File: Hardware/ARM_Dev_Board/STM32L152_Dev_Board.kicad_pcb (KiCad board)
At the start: 2 copper layers, 65.3 x 24.9 mm, 21 parts, among them J1 SWD_Header, J2 Conn_01x20_Female, J3 Conn_01x22_Female, J4 Eurorack_10_pin_power, SW1 SW_Push, U1 STM32L451CCUx, U4 LM1117-3.3, Y1 Crystal

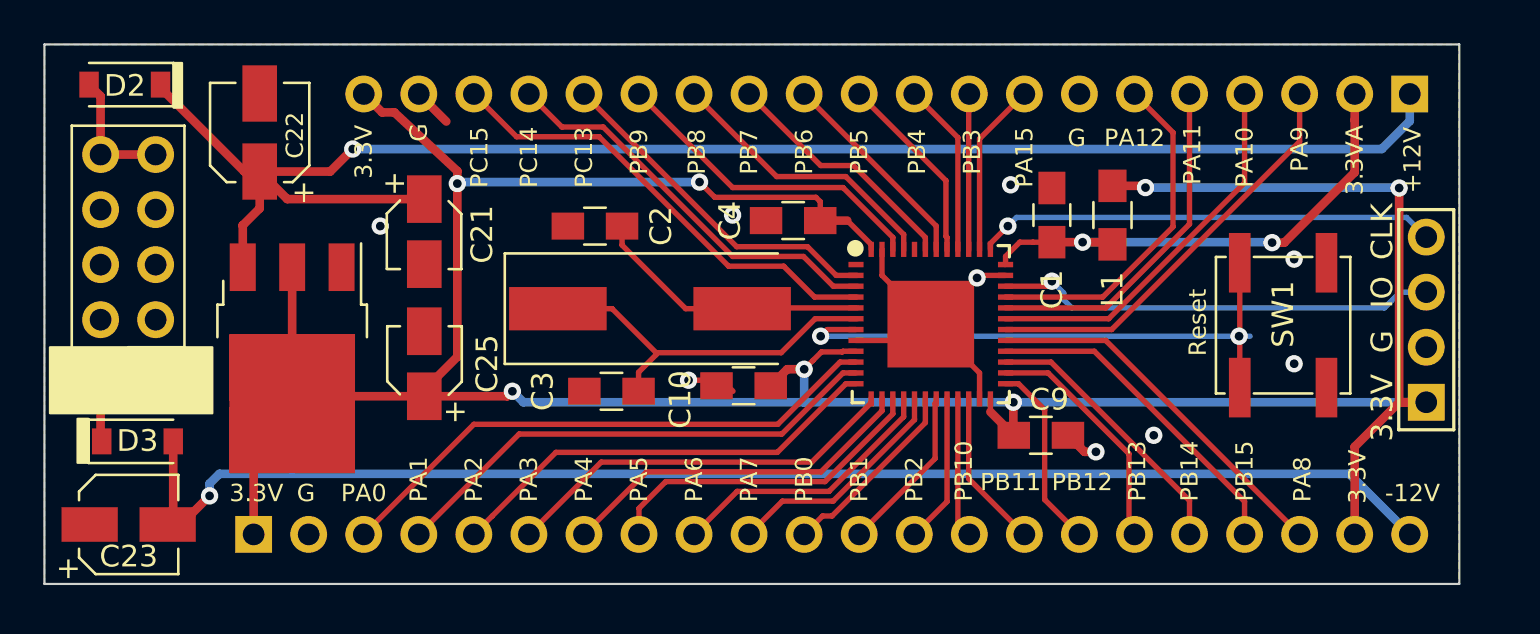
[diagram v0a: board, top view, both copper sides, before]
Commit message: Dev Board 1.1 layout finalised and gerbers sent to manufacturing
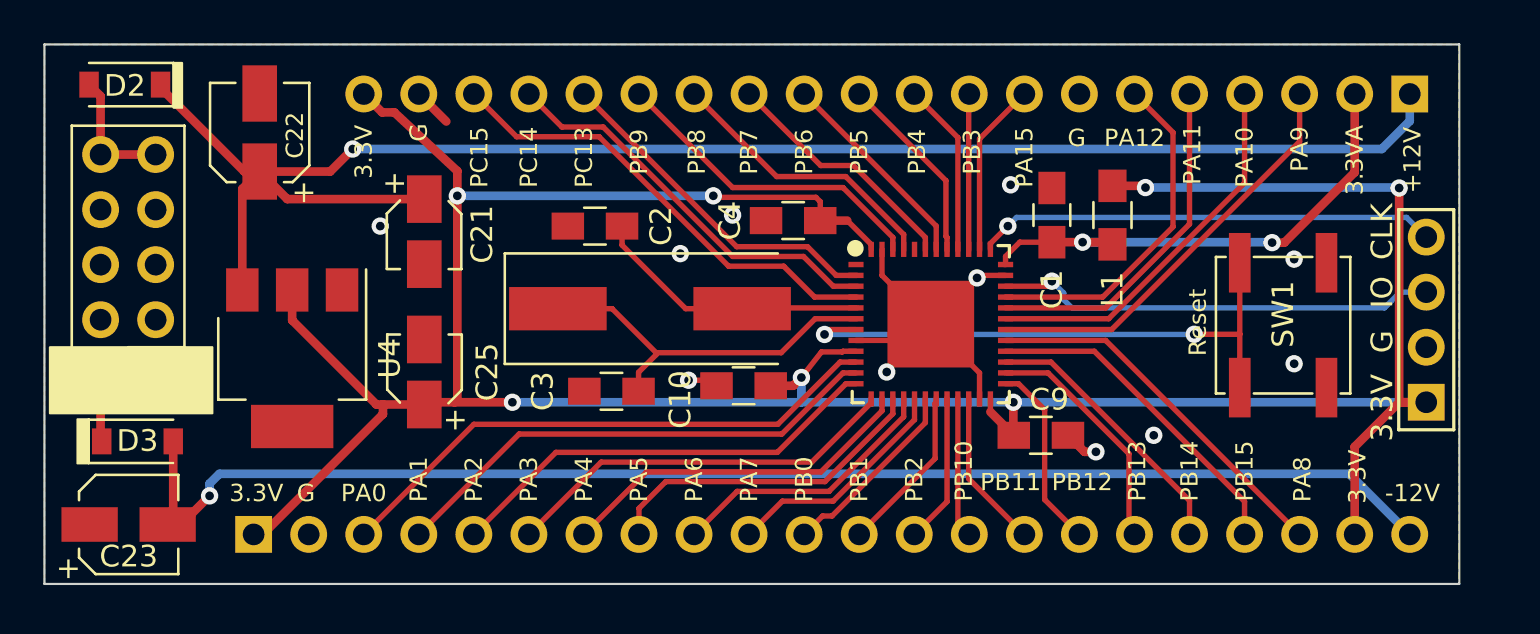
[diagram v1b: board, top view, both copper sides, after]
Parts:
- U4: footprint TO_SOT_Packages_SMD:TO-252-3_TabPin2 -> TO_SOT_Packages_SMD:SOT-223
- moved C25 0.38 mm to (160.3, 141.9)
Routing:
- net +3V3: track 146.3 -> 143.6 mm
- net VCC: track 74.5 -> 75.5 mm
- net Reset: track 27.3 -> 26.5 mm
- net GND: track 14.5 -> 13.8 mm, vias 9 -> 11
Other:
- board text added: "STM32L152 and STM32L451 Dev Board Mountjoy Modular v1.1"
- board text removed: "STM32L152 and STM32L451 Dev Board Mountjoy Modular v1"

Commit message: Added early draft of support for ICE40UP5k FPGA
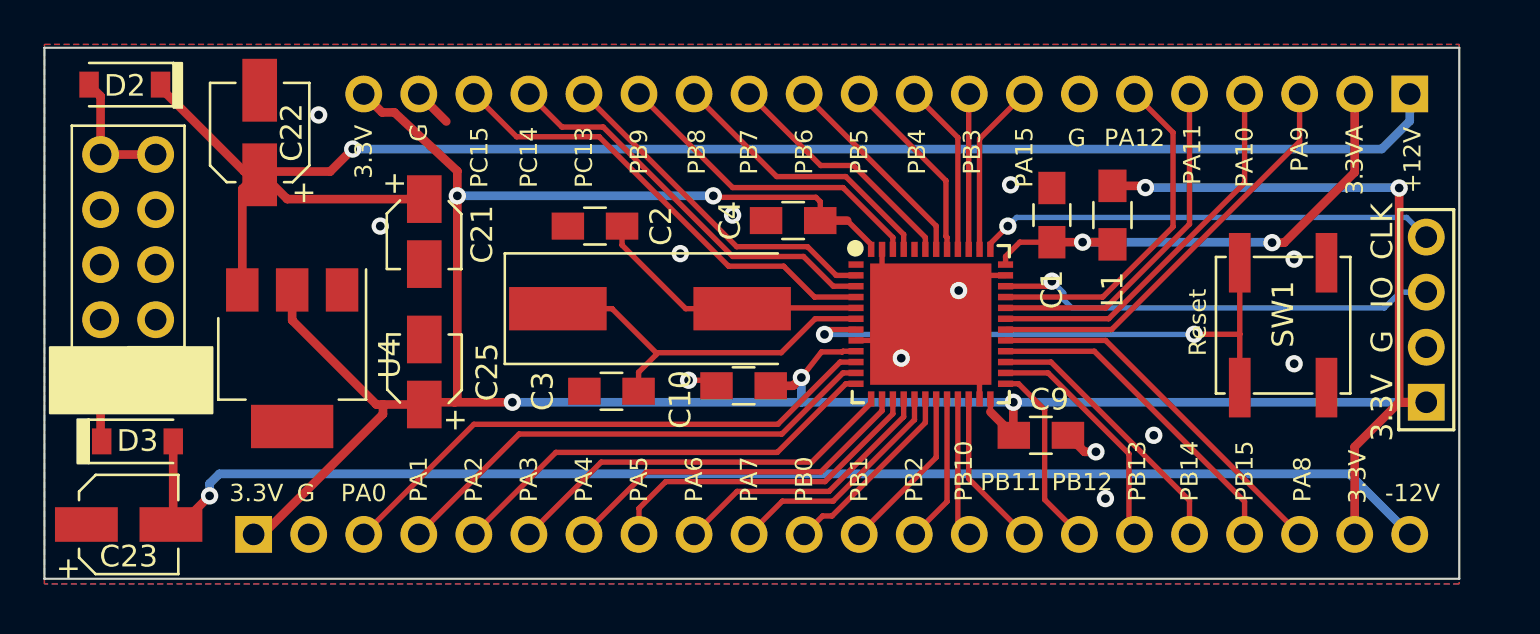
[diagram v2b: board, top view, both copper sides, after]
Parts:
- C22, C23: footprint Capacitors_SMD:CP_Elec_4x5.8 -> Custom_Footprints:CP_Elec_4x5.8_Big_pad
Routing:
- net GND: vias 11 -> 13
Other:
- board size 65.3 x 24.9 mm -> 65.3 x 24.5 mm
- board text added: "STM32L152 and STM32L451 Dev Board Mountjoy Modular v2.0"
- board text removed: "STM32L152 and STM32L451 Dev Board Mountjoy Modular v1.1"

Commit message: Rev 2 of dev board; provisional handling for overflow on output samples
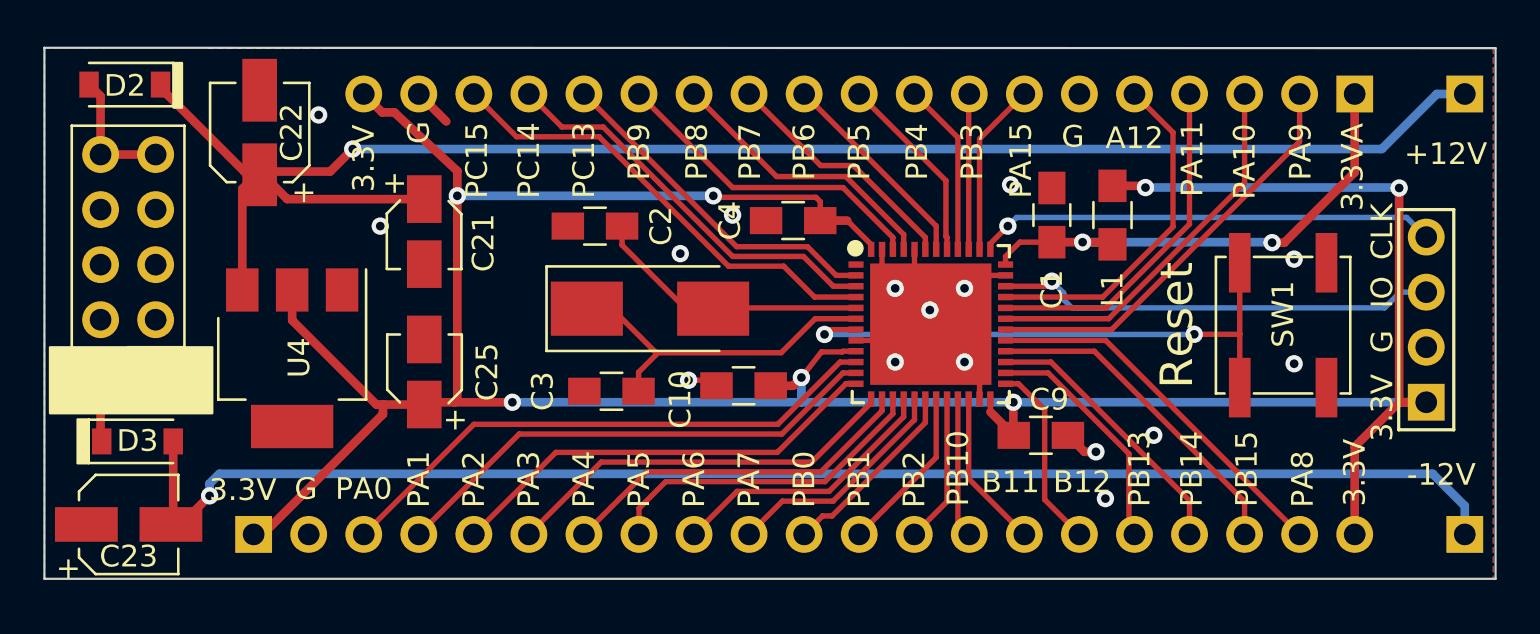
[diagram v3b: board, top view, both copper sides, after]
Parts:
- added J5: Conn_01x01_Female, Pin_Headers:Pin_Header_Straight_1x01_Pitch2.54mm, F.Cu at (208.3, 129.0)
- added J6: Conn_01x01_Female, Pin_Headers:Pin_Header_Straight_1x01_Pitch2.54mm, F.Cu at (208.3, 149.4)
- J2: value Conn_01x20_Female -> Conn_01x19_Female; footprint Pin_Headers:Pin_Header_Straight_1x20_Pitch2.54mm -> Pin_Headers:Pin_Header_Straight_1x19_Pitch2.54mm
- J3: value Conn_01x22_Female -> Conn_01x21_Female; footprint Pin_Headers:Pin_Header_Straight_1x22_Pitch2.54mm -> Pin_Headers:Pin_Header_Straight_1x21_Pitch2.54mm
- Y1: footprint Custom_Footprints:Crystal_SMD -> Crystals:Crystal_SMD_0603-2pin_6.0x3.5mm_HandSoldering
- moved J2 2.54 mm to (203.2, 129.0)
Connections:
- J2 pad 1: VCC -> +3.3VA
- J2 pad 10: PB4 -> PB5
- J2 pad 11: PB5 -> PB6
- J2 pad 12: PB6 -> PB7
- J2 pad 13: PB7 -> PB8
- J2 pad 14: PB8 -> PB9
- J2 pad 15: PB9 -> PC13
- J2 pad 16: PC13 -> PC14
- J2 pad 17: PC14 -> PC15
- J2 pad 18: PC15 -> GND
- J2 pad 19: GND -> +3V3
- J2 pad 2: +3.3VA -> PA9
- J2 pad 3: PA9 -> PA10
- J2 pad 4: PA10 -> PA11
- J2 pad 5: PA11 -> PA12
- J2 pad 6: PA12 -> GND
- J2 pad 7: GND -> PA15
- J2 pad 8: PA15 -> PB3
- J2 pad 9: PB3 -> PB4
- U1 pad 44: Net-(U1-Pad44) -> GND
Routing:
- net VEE: track 63.7 -> 67.0 mm
- net GND: track 13.8 -> 15.9 mm, vias 13 -> 16
- net VCC: track 75.5 -> 77.3 mm
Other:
- board size 65.3 x 24.5 mm -> 67 x 24.5 mm
- board text added: "A12"
- board text added: "B11"
- board text added: "B12"
- board text removed: "PA12"
- board text removed: "PB11"
- board text removed: "PB12"

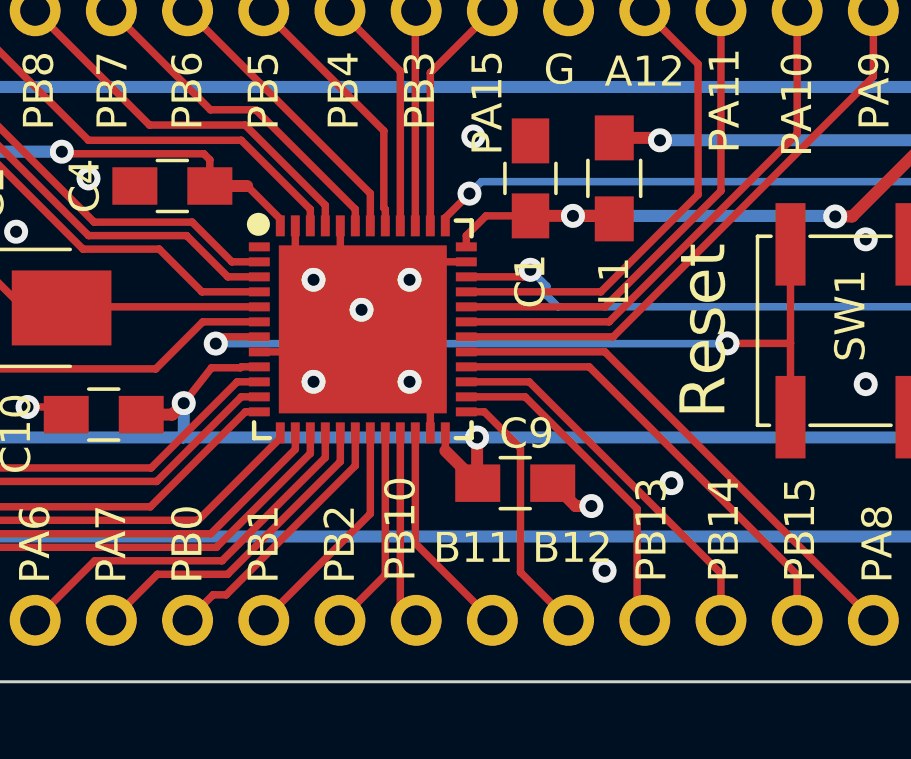
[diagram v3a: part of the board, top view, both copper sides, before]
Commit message: Fixes to schematic (missing resistor on 1.2V LDO); Created new implementation to support production board; added FPGA tester project
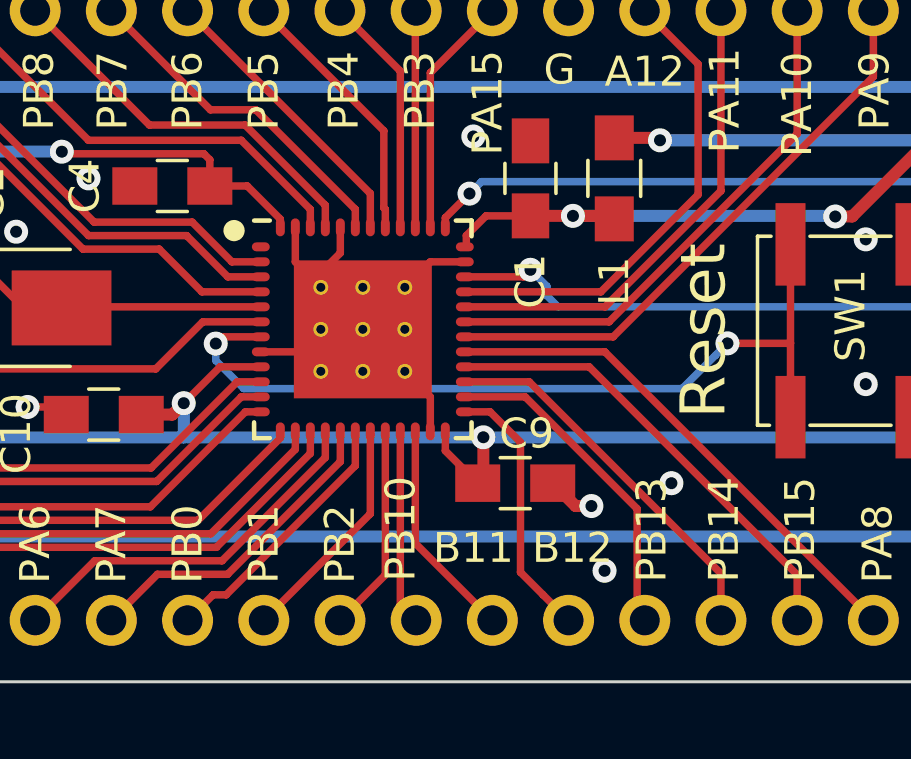
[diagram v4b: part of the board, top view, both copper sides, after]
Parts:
- U1: footprint Custom_Footprints:ARM-UQFN-48-7x7mm_Pitch0.5mm -> Custom_Footprints:ICE40_QFN-48-1EP_7x7mm_Pitch0.5mm
- turned U1 to 90 degrees
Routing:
- net Reset: track 26.5 -> 28.1 mm
- net GND: track 15.9 -> 15.4 mm, vias 16 -> 11
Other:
- board text added: "STM32L152 and STM32L451 Dev Board Mountjoy Modular v3.0"
- board text removed: "STM32L152 and STM32L451 Dev Board Mountjoy Modular v2.0"
